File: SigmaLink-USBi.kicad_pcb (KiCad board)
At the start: 2 copper layers, 64 x 39 mm, 38 parts, among them J1 USB_B, J2 Program, J3 Target, U1 LM1117-3.3, U2 24LC512, U3 CY7C68013A-56, U4 MAX809, U5 74LVC2G66, U6 TPS2051B, Y1 24MHz

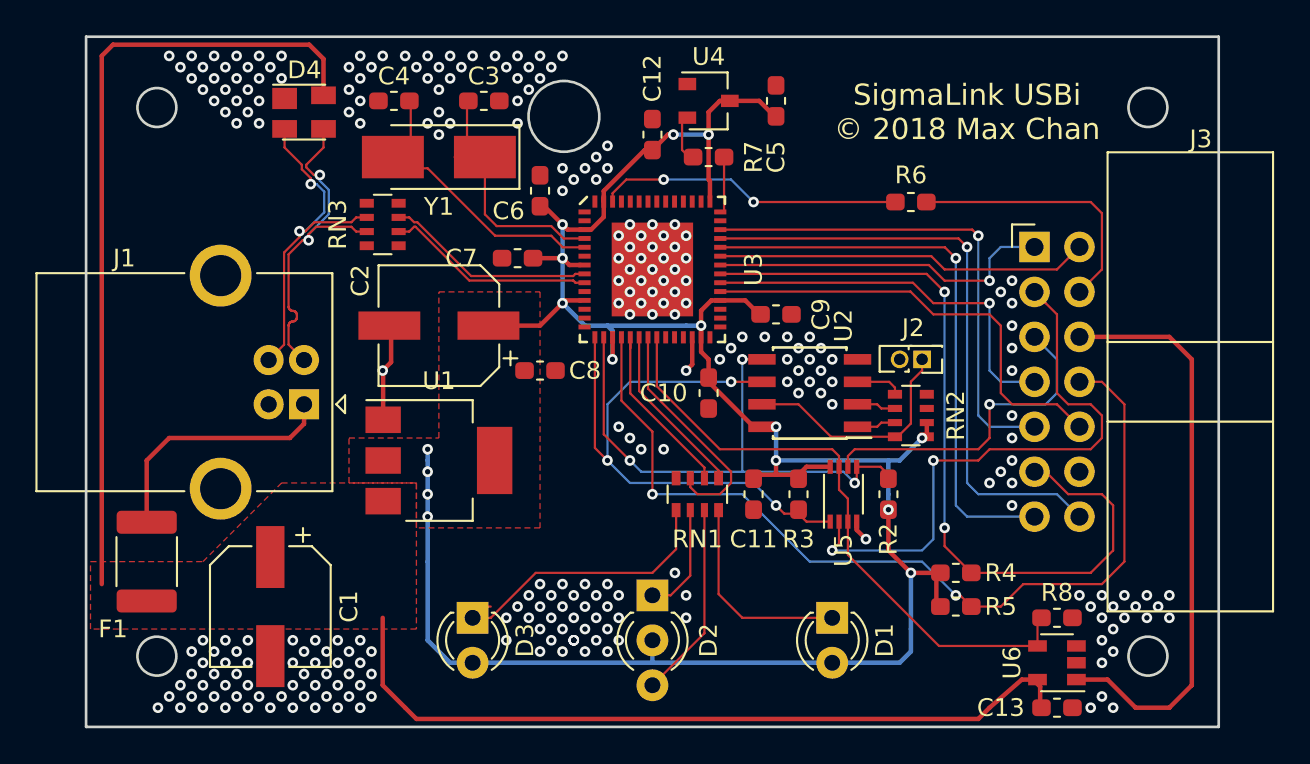
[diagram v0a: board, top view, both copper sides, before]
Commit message: Resistor packs are used more extensively.
Also a re-layout.
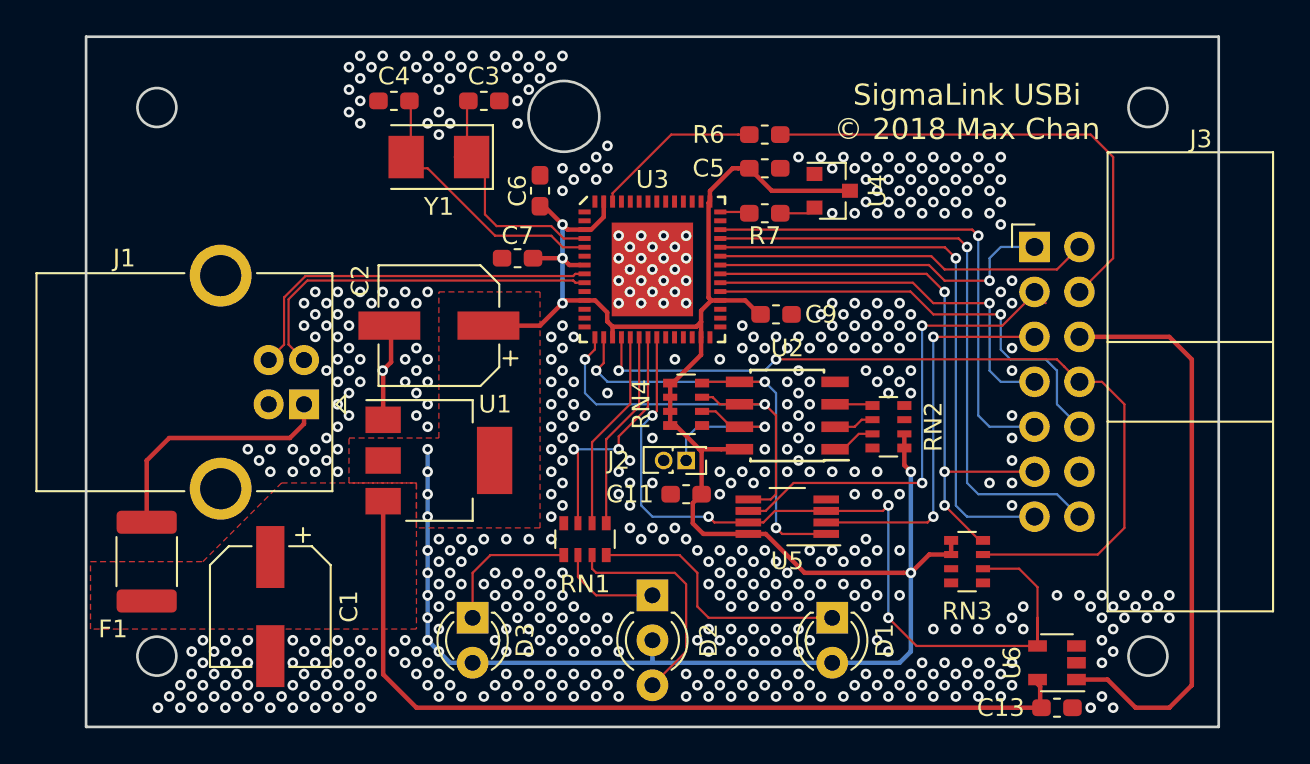
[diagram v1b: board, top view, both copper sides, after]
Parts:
- removed C10, C12, C8: 100n, Capacitor_SMD:C_0603_1608Metric_Pad1.05x0.95mm_HandSolder
- removed D4: PRTR5V0U2X, Package_TO_SOT_SMD:SOT-143
- removed R2, R3: 4.7k, Resistor_SMD:R_0603_1608Metric_Pad1.05x0.95mm_HandSolder
- removed R4, R5, R8: 10k, Resistor_SMD:R_0603_1608Metric_Pad1.05x0.95mm_HandSolder
- added RN4: 4.7k, Resistor_SMD:R_Array_Convex_4x0603, F.Cu at (151.9, 101.3)
- RN3: value 22 -> 10k
- U4: footprint Package_TO_SOT_SMD:SOT-23W -> Package_TO_SOT_SMD:SOT-23
- U5: footprint Package_SO:VSSOP-8_2.3x2mm_P0.5mm -> Package_SO:VSSOP-8_3.0x3.0mm_P0.65mm
- Y1: footprint Crystal:Crystal_SMD_5032-2Pin_5.0x3.2mm_HandSoldering -> Crystal:Crystal_SMD_5032-2Pin_5.0x3.2mm
- moved RN3 38.1 mm to (167.8, 110.2), turned to 180 degrees
- moved J2 14.5 mm to (151.9, 104.4)
- moved R6 9.09 mm to (156.3, 86.0)
- moved U4 8.64 mm to (160.2, 89.2)
- moved RN1 6.84 mm to (146.2, 108.9)
- moved R7 4.49 mm to (156.3, 90.5), turned to 180 degrees
- moved C5 3.86 mm to (156.3, 87.9), turned to 0 degrees
- moved C11 3.81 mm to (151.9, 106.3), turned to 180 degrees
- moved U5 3.42 mm to (157.6, 107.6), turned to 180 degrees
- moved U2 1.80 mm to (157.6, 101.9)
- moved RN2 1.42 mm to (163.3, 102.5)
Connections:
- J1 pad 2: /UD- -> /D-
- J1 pad 3: /UD+ -> /D+
- RN2 pad 8: Net-(J2-Pad1) -> (no net)
- RN3 pad 2: /UD+ -> /USB_EN
- RN3 pad 3: /UD- -> /TRESET
- RN3 pad 4: (no net) -> /~TLATCH1
- RN3 pad 5: (no net) -> +3V3
- RN3 pad 6: /D- -> +3V3
- RN3 pad 7: /D+ -> GND
- RN3 pad 8: (no net) -> GND
- U5 pad 1: /SCL -> /SDA
- U5 pad 2: /TSCL -> /TSDA
- U5 pad 5: /SDA -> /SCL
- U5 pad 6: /TSDA -> /TSCL
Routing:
- net +5V: track 89.0 -> 49.6 mm
- net /UD-: track 20.1 -> 0.00 mm, vias 2 -> 0
- net /UD+: track 19.8 -> 0.00 mm, vias 2 -> 0
- net /USB_EN: track 34.6 -> 48.2 mm, vias 0 -> 4
- net /TMCLK: track 15.2 -> 27.7 mm
- net /~TLATCH1: track 46.3 -> 33.9 mm, vias 2 -> 3
- net /D+: track 11.9 -> 21.4 mm
- net /D-: track 11.9 -> 21.0 mm
- net /SCL: track 33.5 -> 24.5 mm, vias 3 -> 2
- net Net-(D3-Pad1): track 16.5 -> 8.11 mm
- net /MCK: track 17.3 -> 9.57 mm, vias 2 -> 0
- net /TSCL: track 32.8 -> 27.5 mm
- net /TRESET: track 51.7 -> 47.5 mm
- net /SDA: track 31.0 -> 26.9 mm
- net Net-(D1-Pad1): track 11.7 -> 15.4 mm
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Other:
- rule pad_to_mask_clearance: 0.2 -> 0
